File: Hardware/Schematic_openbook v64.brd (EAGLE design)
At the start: 170.2 x 111.2 mm, 103 parts, among them IC1 BD5229G-TR, IC4 XC6220A331MR-G, J1 FH34SRJ-24S-0.5SH_99_, J2 SAMACSYS_PARTS_USB4110-GF-A, J3 QWIIC_RIGHT_ANGLE, J4 112A-TAAR-R03_ATTEND, Q1 20V/4.2A/52mΩ/1.4W, Q2 20V/4.2A/52mΩ/1.4W, Q3 SI1308EDL-T1-GE3, U1 W25Q512JVEIQ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

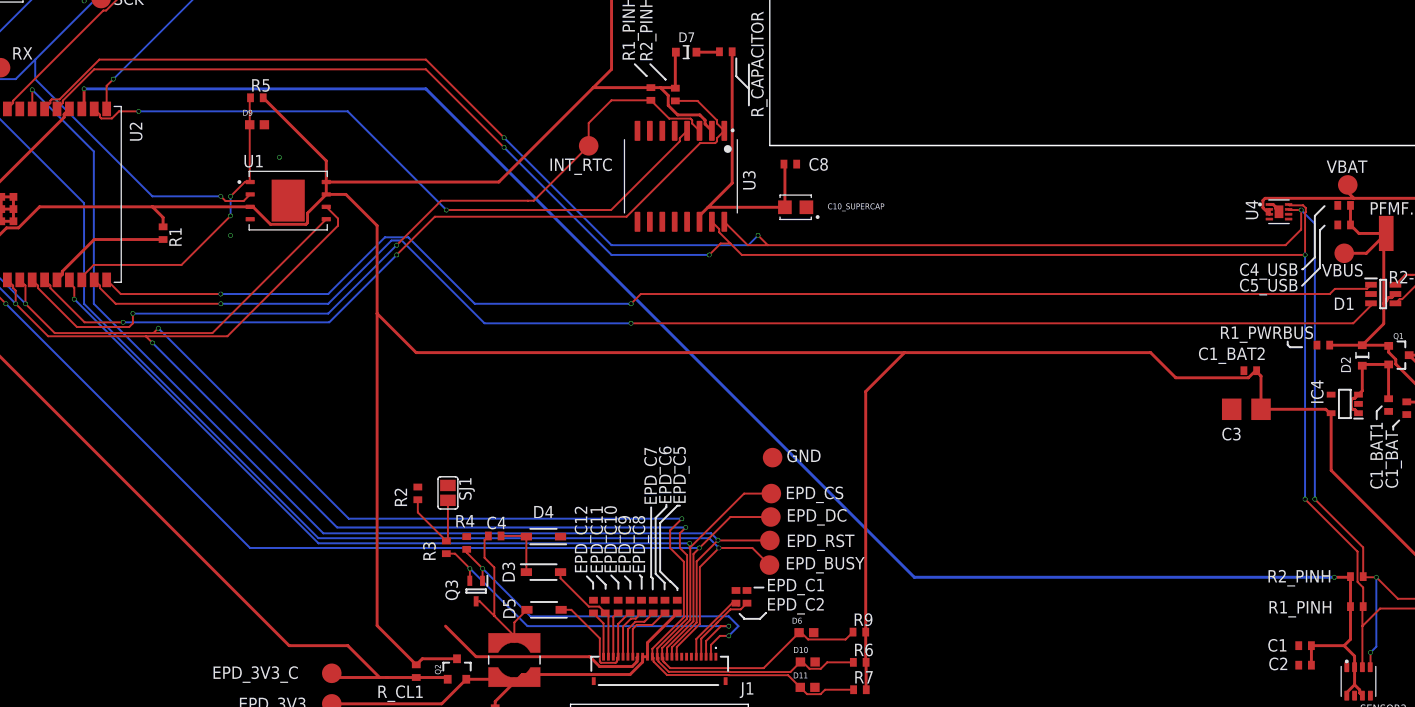
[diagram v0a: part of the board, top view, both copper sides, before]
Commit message: Missing via stiching to a component
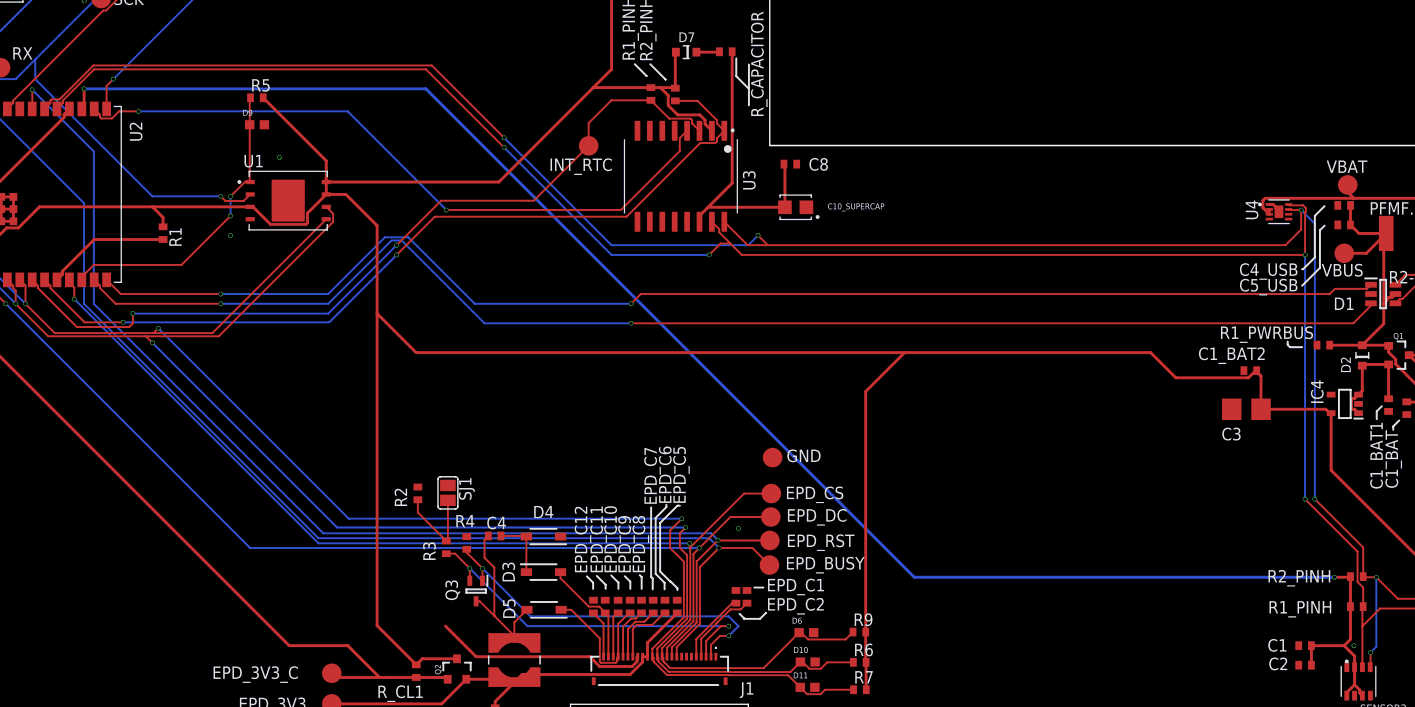
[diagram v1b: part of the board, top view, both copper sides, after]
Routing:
- net SCK: track 223.0 -> 222.1 mm
- net RTC_RST: track 69.3 -> 69.9 mm
- net GND: vias 10 -> 12
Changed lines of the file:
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@@
 <layer number="14" name="Route14" color="22" fill="1" visible="no" active="no"/>
 <layer number="15" name="Route15" color="23" fill="1" visible="no" active="no"/>
-<layer number="16" name="Bottom" color="1" fill="1" visible="yes" active="yes"/>
+<layer number="16" name="Bottom" color="1" fill="1" visible="no" active="yes"/>
 <layer number="17" name="Pads" color="2" fill="1" visible="yes" active="yes"/>
 <layer number="18" name="Vias" color="2" fill="1" visible="yes" active="yes"/>
@@
 <wire x1="165.07" y1="50.292" x2="165.07" y2="49.107" width="0.3" layer="1"/>
 <contactref element="D1" pad="2"/>
+<via x="89" y="28" extent="1-16" drill="0.35" alwaysstop="yes">
+</via>
+<via x="152" y="16" extent="1-16" drill="0.35" alwaysstop="yes">
+</via>
 </signal>
 <signal name="SS_SD">
@@
 <wire x1="7.673" y1="56.527" x2="7.673" y2="81.773" width="0.2" layer="16"/>
 <wire x1="7.673" y1="81.773" x2="18.6" y2="92.7" width="0.2" layer="16"/>
-<wire x1="48" y1="59" x2="48" y2="59.72" width="0.2" layer="1"/>
-<wire x1="48" y1="59.72" x2="46.795" y2="60.925" width="0.2" layer="1"/>
 <wire x1="15" y1="51" x2="18.327" y2="47.673" width="0.2" layer="1"/>
 <wire x1="18.327" y1="47.673" x2="28.327" y2="47.673" width="0.2" layer="1"/>
-<wire x1="28.327" y1="47.673" x2="36.673" y2="47.673" width="0.2" layer="1"/>
-<wire x1="36.673" y1="47.673" x2="48" y2="59" width="0.2" layer="1"/>
 <via x="29" y="47" extent="1-16" drill="0.35" alwaysstop="yes">
 </via>
@@
 <wire x1="47.9" y1="28.1" x2="29" y2="47" width="0.2" layer="16"/>
 <wire x1="29" y1="47" x2="28.327" y2="47.673" width="0.2" layer="1"/>
+<wire x1="47.492" y1="60.228" x2="46.795" y2="60.925" width="0.2" layer="1"/>
+<wire x1="47.492" y1="59.37319375" x2="47.492" y2="60.228" width="0.2" layer="1"/>
+<wire x1="28.327" y1="47.673" x2="35.79180625" y2="47.673" width="0.2" layer="1"/>
+<wire x1="35.79180625" y1="47.673" x2="47.492" y2="59.37319375" width="0.2" layer="1"/>
 </signal>
 <signal name="3V3">
@@
 <via x="87" y="26" extent="1-16" drill="0.35" alwaysstop="yes">
 </via>
-<wire x1="85.042" y1="24.042" x2="87" y2="26" width="0.2" layer="1"/>
-<wire x1="87" y1="26" x2="90.42" y2="26" width="0.2" layer="1"/>
-<wire x1="90.42" y1="26" x2="92.17" y2="24.25" width="0.2" layer="1"/>
+<wire x1="87" y1="26" x2="85.042" y2="24.042" width="0.2" layer="1"/>
+<wire x1="90.42" y1="26" x2="87" y2="26" width="0.2" layer="1"/>
+<wire x1="92.17" y1="24.25" x2="90.42" y2="26" width="0.2" layer="1"/>
 <via x="10.3" y="73" extent="1-16" drill="0.35" alwaysstop="yes">
 </via>
@@
 <wire x1="46" y1="27" x2="22" y2="51" width="0.2" layer="16"/>
 <wire x1="86" y1="27" x2="46" y2="27" width="0.2" layer="16"/>
-<wire x1="87" y1="26" x2="86" y2="27" width="0.2" layer="16"/>
+<wire x1="86" y1="27" x2="87" y2="26" width="0.2" layer="16"/>
 </signal>
 <signal name="EPD_DC">
@@
 <wire x1="84.388" y1="25.388" x2="85" y2="26" width="0.2" layer="1"/>
 <wire x1="85" y1="26" x2="88.17" y2="29.17" width="0.2" layer="1"/>
-<wire x1="88.17" y1="29.17" x2="92.31" y2="29.17" width="0.2" layer="1"/>
+<wire x1="92.31" y1="29.17" x2="88.17" y2="29.17" width="0.2" layer="1"/>
 <wire x1="85" y1="26" x2="39" y2="26" width="0.2" layer="16"/>
 <wire x1="39" y1="26" x2="14" y2="51" width="0.2" layer="16"/>
@@
 <wire x1="27.6" y1="70.7" x2="49" y2="70.7" width="0.2" layer="16"/>
 <wire x1="49" y1="70.7" x2="59.1" y2="60.6" width="0.2" layer="16"/>
-<wire x1="82.987" y1="67.629175" x2="82.987" y2="67.957" width="0.2" layer="1"/>
+<wire x1="82.987" y1="66.629175" x2="82.987" y2="67.957" width="0.2" layer="1"/>
 <wire x1="82.987" y1="67.957" x2="83.735" y2="68.705" width="0.2" layer="1"/>
-<wire x1="59.1" y1="60.6" x2="75.957825" y2="60.6" width="0.2" layer="1"/>
-<wire x1="75.957825" y1="60.6" x2="82.987" y2="67.629175" width="0.2" layer="1"/>
+<wire x1="59.1" y1="60.6" x2="76.957825" y2="60.6" width="0.2" layer="1"/>
+<wire x1="76.957825" y1="60.6" x2="82.987" y2="66.629175" width="0.2" layer="1"/>
 </signal>
 <signal name="I2C_PW">
@@
 <wire x1="18.553" y1="71.794025" x2="18.685975" y2="71.927" width="0.2" layer="1"/>
 <wire x1="18.685975" y1="71.927" x2="19.493525" y2="71.927" width="0.2" layer="1"/>
-<wire x1="19.493525" y1="71.927" x2="23.566525" y2="76" width="0.2" layer="1"/>
-<wire x1="23.566525" y1="76" x2="57" y2="76" width="0.2" layer="1"/>
-<wire x1="57" y1="76" x2="65" y2="68" width="0.2" layer="1"/>
+<wire x1="19.493525" y1="71.927" x2="22.966525" y2="75.4" width="0.2" layer="1"/>
+<wire x1="22.966525" y1="75.4" x2="57.6" y2="75.4" width="0.2" layer="1"/>
+<wire x1="57.6" y1="75.4" x2="65" y2="68" width="0.2" layer="1"/>
 <via x="91" y="58" extent="1-16" drill="0.35" alwaysstop="yes">
 </via>
@@
 <via x="86.9" y="26.8" extent="1-16" drill="0.35" alwaysstop="yes">
 </via>
-<wire x1="84.715" y1="24.615" x2="86.9" y2="26.8" width="0.2" layer="1"/>
-<wire x1="86.9" y1="26.8" x2="86.93" y2="26.77" width="0.2" layer="1"/>
-<wire x1="86.93" y1="26.77" x2="92.21" y2="26.77" width="0.2" layer="1"/>
+<wire x1="86.9" y1="26.8" x2="84.715" y2="24.615" width="0.2" layer="1"/>
+<wire x1="86.93" y1="26.77" x2="86.9" y2="26.8" width="0.2" layer="1"/>
+<wire x1="92.21" y1="26.77" x2="86.93" y2="26.77" width="0.2" layer="1"/>
 <via x="16.7" y="72.9" extent="1-16" drill="0.35" alwaysstop="yes">
 </via>
